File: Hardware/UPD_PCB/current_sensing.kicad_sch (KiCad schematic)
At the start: 66 parts, among them IC1 STS30-DIS, Q7 BSS84, U1 ACS711xEXLT-31AB, U2 INA219AxD, U3 INA219AxD, U4 INA219AxD, U5 INA219AxD, U6 INA219AxD, U7 INA219AxD

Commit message: Version 1.1 of PCB
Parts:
- R13, R26, R27, R36, R37: value 0.2R -> 0.1R
- R14: value 2mR -> 0.1R
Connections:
- net +5V: now also U5.1 (A1)
- net INA_SCL: no longer U5.1 (A1)
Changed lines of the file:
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@@
 	)
 	(junction
-		(at 210.82 144.78)
-		(diameter 0)
-		(color 0 0 0 0)
-	)
-	(junction
 		(at 123.19 191.77)
 		(diameter 0)
@@
 	(wire
 		(pts
-			(xy 203.2 143.51) (xy 210.82 143.51)
+			(xy 203.2 143.51) (xy 217.17 143.51)
 		)
 		(stroke
@@
 	(wire
 		(pts
-			(xy 210.82 144.78) (xy 217.17 144.78)
-		)
-		(stroke
-			(width 0)
-			(type default)
-		)
-	)
-	(wire
-		(pts
 			(xy 290.83 143.51) (xy 290.83 144.78)
 		)
@@
 	(wire
 		(pts
-			(xy 203.2 146.05) (xy 210.82 146.05)
+			(xy 203.2 146.05) (xy 217.17 146.05)
 		)
 		(stroke
@@
 	(wire
 		(pts
-			(xy 210.82 143.51) (xy 210.82 144.78)
-		)
-		(stroke
-			(width 0)
-			(type default)
-		)
-	)
-	(wire
-		(pts
 			(xy 179.07 76.2) (xy 182.88 76.2)
 		)
@@
 	(wire
 		(pts
-			(xy 210.82 144.78) (xy 210.82 146.05)
-		)
-		(stroke
-			(width 0)
-			(type default)
-		)
-	)
-	(wire
-		(pts
 			(xy 292.1 124.46) (xy 292.1 123.19)
 		)
@@
 	(global_label "INA_SCL"
 		(shape input)
-		(at 217.17 144.78 0)
+		(at 217.17 146.05 0)
 		(fields_autoplaced yes)
 		(effects
@@
 		)
 		(property "Intersheetrefs" "${INTERSHEET_REFS}"
-			(at 227.6543 144.78 0)
+			(at 227.6543 146.05 0)
 			(effects
 				(font
@@
 			)
 		)
-		(property "Value" "0.2R"
+		(property "Value" "0.1R"
 			(at 162.56 77.724 90)
 			(effects
@@
 			)
 		)
-		(property "Value" "0.2R"
+		(property "Value" "0.1R"
 			(at 162.56 138.684 90)
 			(effects
@@
 			)
 		)
-		(property "Value" "0.2R"
+		(property "Value" "0.1R"
 			(at 243.84 77.724 90)
 			(effects
@@
 			)
 		)
-		(property "Value" "2mR"
+		(property "Value" "0.1R"
 			(at 81.28 138.684 90)
 			(effects
@@
 			)
 		)
-		(property "Value" "0.2R"
+		(property "Value" "0.1R"
 			(at 242.57 138.684 90)
 			(effects
@@
 			)
 		)
-		(property "Value" "0.2R"
+		(property "Value" "0.1R"
 			(at 81.28 77.724 90)
 			(effects
@@
 					(unit 1)
 				)
+			)
+		)
+	)
+	(symbol
+		(lib_id "power:+5V")
+		(at 217.17 143.51 270)
+		(unit 1)
+		(exclude_from_sim no)
+		(in_bom yes)
+		(on_board yes)
+		(dnp no)
+		(fields_autoplaced yes)
+		(property "Reference" "#PWR090"
+			(at 213.36 143.51 0)
+			(effects
+				(font
+					(size 1.27 1.27)
+				)
+				(hide yes)
+			)
+		)
+		(property "Value" "+5V"
+			(at 220.98 143.5099 90)
+			(effects
+				(font
+					(size 1.27 1.27)
+				)
+				(justify left)
+			)
+		)
+		(property "Footprint" ""
+			(at 217.17 143.51 0)
+			(effects
+				(font
+					(size 1.27 1.27)
+				)
+				(hide yes)
+			)
+		)
+		(property "Datasheet" ""
+			(at 217.17 143.51 0)
+			(effects
+				(font
+					(size 1.27 1.27)
+				)
+				(hide yes)
+			)
+		)
+		(property "Description" "Power symbol creates a global label with name \"+5V\""
+			(at 217.17 143.51 0)
+			(effects
+				(font
+					(size 1.27 1.27)
+				)
+				(hide yes)
+			)
+		)
+		(pin "1"
+		)
+		(instances
+			(project "UPD_PCB"
+				(path "/0650c7a8-acba-429c-9f8e-eec0baf0bc1c/fede4c36-00cc-4d3d-b71c-5243ba232202/7d5a1283-086b-46b0-8df7-a9850521fb5e/345694a5-7ad0-48c3-90e6-5cd4faf10d65"
+					(reference "#PWR090")
+					(unit 1)
+				)

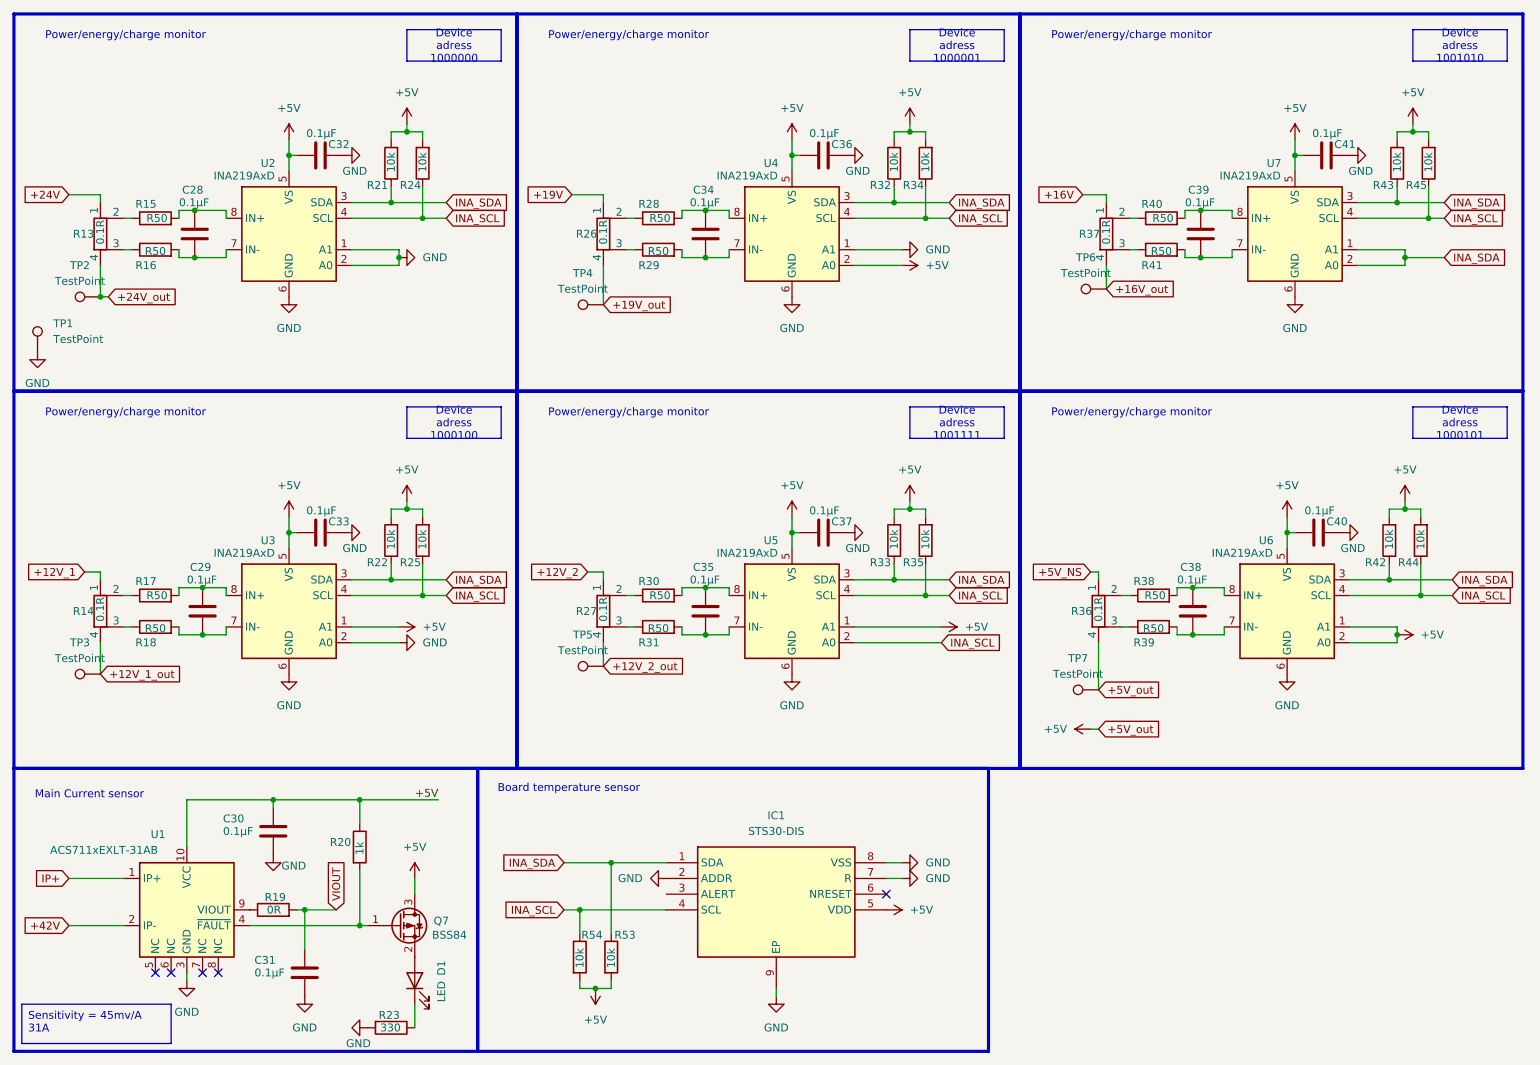
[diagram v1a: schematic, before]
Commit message: Full system monitoring of PCB
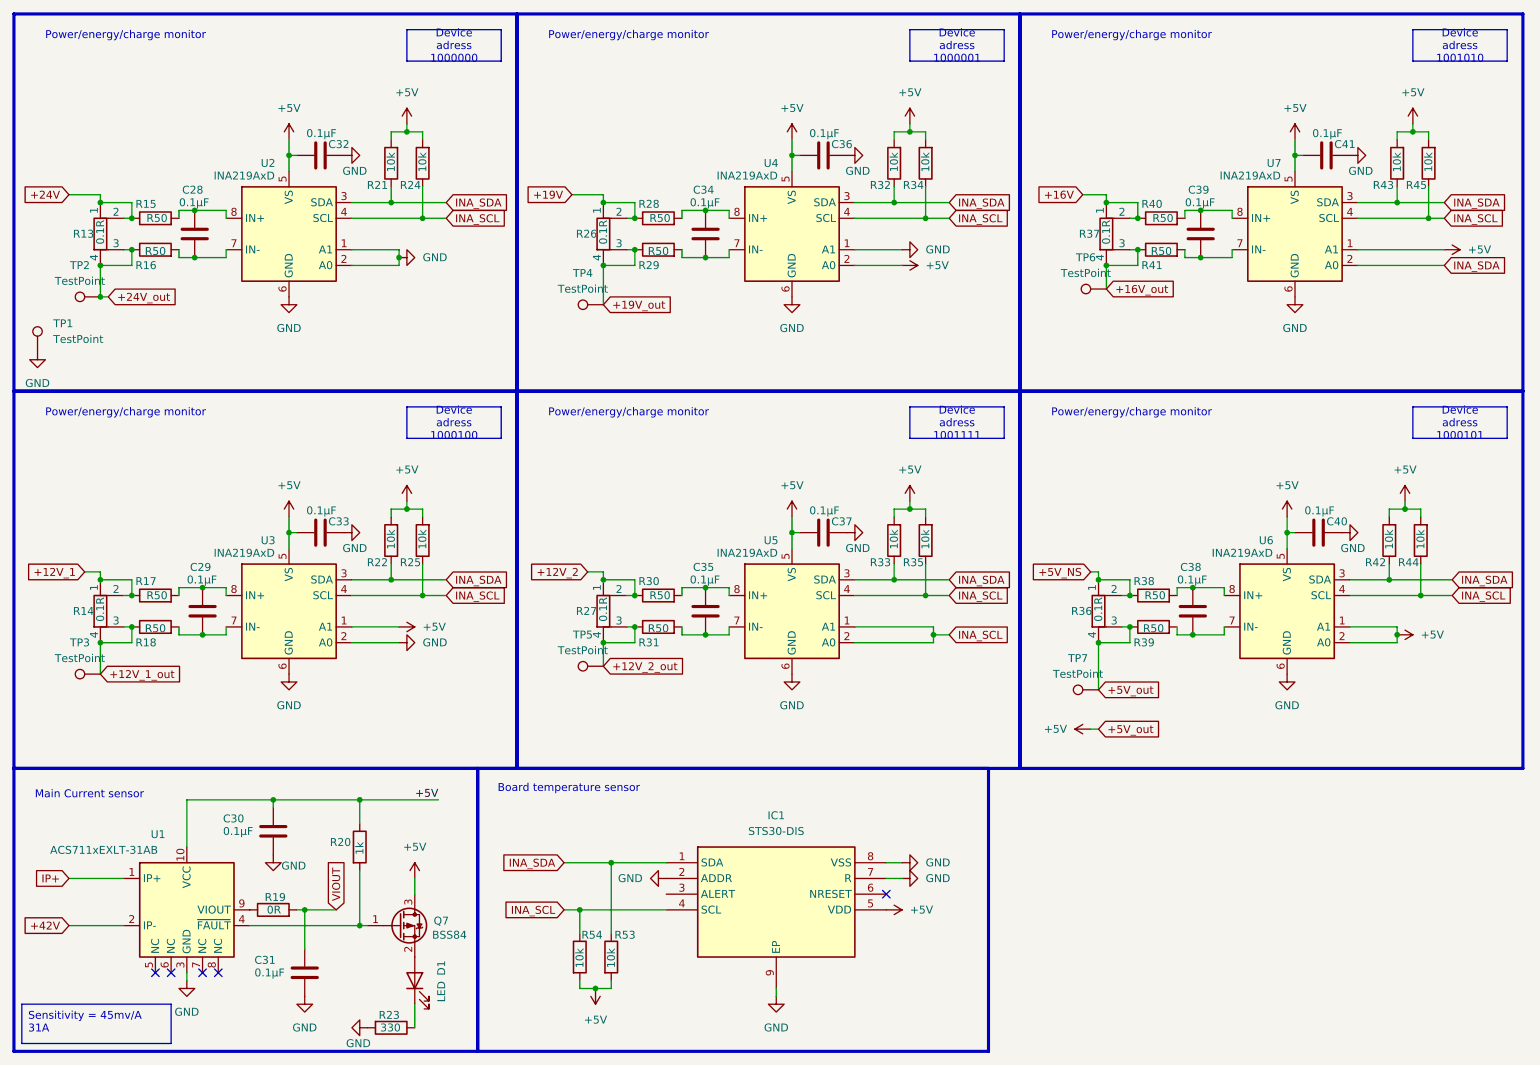
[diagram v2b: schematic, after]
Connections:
- net +12V_1: now also R14.2, R17.1
- net +12V_1_out: now also R14.3, R18.1
- net +12V_2: now also R27.2, R30.1
- net +12V_2_out: now also R27.3, R31.1
- net +16V: now also R37.2, R40.1
- net +16V_out: now also R37.3, R41.1
- net +19V: now also R26.2, R28.1
- net +19V_out: now also R26.3, R29.1
- net +24V: now also R13.2, R15.1
- net +24V_out: now also R13.3, R16.1
- net +5V: now also R36.3, R39.1, U7.1 (A1); no longer U5.1 (A1)
- net +5V_NS: now also R36.2, R38.1
- net INA_SCL: now also U5.1 (A1)
- net INA_SDA: no longer U7.1 (A1)
